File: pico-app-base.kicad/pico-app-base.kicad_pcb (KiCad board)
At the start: 2 copper layers, 53.1 x 61.5 mm, 38 parts, among them J1 Conn_EYESPI, J5 Stemma-QT_Qwicc, J7 JST-PH2 Bat, J9 Alt Bat, Q1 AO3401A, Q2 AO3401A, SW1 SW_ON, SW2 SW_ON, SW3 SW_RST, U1 PCF8563T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

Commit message: added zones and connections
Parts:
- moved SW3 39.0 mm to (125.6, 110.7), turned to 0 degrees
- moved SW1 38.5 mm to (125.6, 102.8), turned to 0 degrees
- moved J1 27.7 mm to (150.2, 134.1), turned to 180 degrees
- moved J5 8.12 mm to (171.3, 79.2), turned to 180 degrees
- moved H2 7.00 mm to (172.4, 86.1)
- moved R3 4.35 mm to (164.8, 87.5)
- moved R4 4.30 mm to (164.8, 85.0)
- moved J7 2.30 mm to (128.3, 96.3)
- moved J9 2.30 mm to (128.7, 97.8)
- moved JP3 1.33 mm to (127.8, 87.8)
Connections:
- C1 pad 1: +BAT -> +BATT
- C2 pad 1: +BAT -> +BATT
- J7 pad 1: +BATT -> Net-(J7-Pin_1)
- J9 pad 1: +BATT -> Net-(J7-Pin_1)
- JP3 pad 1: +BAT -> Net-(J7-Pin_1)
- Q2 pad 2: +BAT -> +BATT
- R2 pad 1: +BAT -> +BATT
- SW2 pad 3: +BAT -> Net-(J7-Pin_1)
- U1 pad 8: +BAT -> +BATT
- U2 pad 7: +BAT -> +BATT
- U2 pad 8: +BAT -> +BATT
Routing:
- net GND: track 0.00 -> 101.2 mm, vias 0 -> 21
- net +3V3: track 112.2 -> 180.7 mm, vias 0 -> 4
- net ~{INT}: track 8.06 -> 42.1 mm
- net +BATT: track 30.5 -> 50.0 mm, vias 0 -> 7
- net Net-(J7-Pin_1): track 0.00 -> 17.3 mm
- net RUN: track 0.00 -> 16.2 mm
- net +BAT: track 8.40 -> 0.00 mm
- net VBUS: track 17.3 -> 12.4 mm, vias 0 -> 6
- net SCL: track 14.8 -> 18.7 mm, vias 3 -> 1
- net SDA: track 14.9 -> 17.8 mm, vias 0 -> 2
- net -BATT: track 16.2 -> 13.9 mm
- net Display_CS: track 0.00 -> 1.69 mm
- net MISO0: track 34.5 -> 36.1 mm
- added copper zone on B.Cu, net +BATT
- added copper zone on F.Cu, net +BATT
- added copper zone on F.Cu, net GND
- added copper zone on B.Cu, net VBUS
- added copper zone on F.Cu, net VBUS

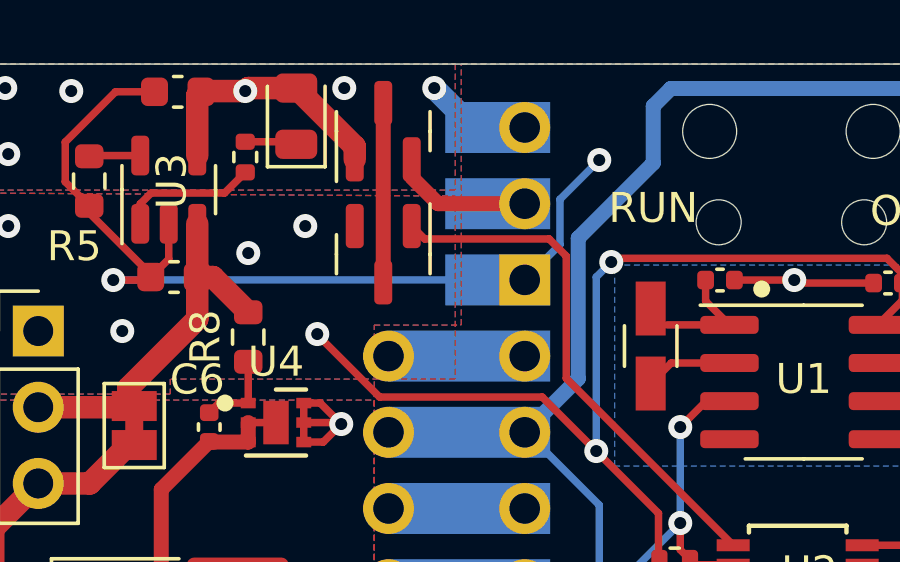
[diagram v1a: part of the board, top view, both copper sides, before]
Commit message: switched order of mosfets
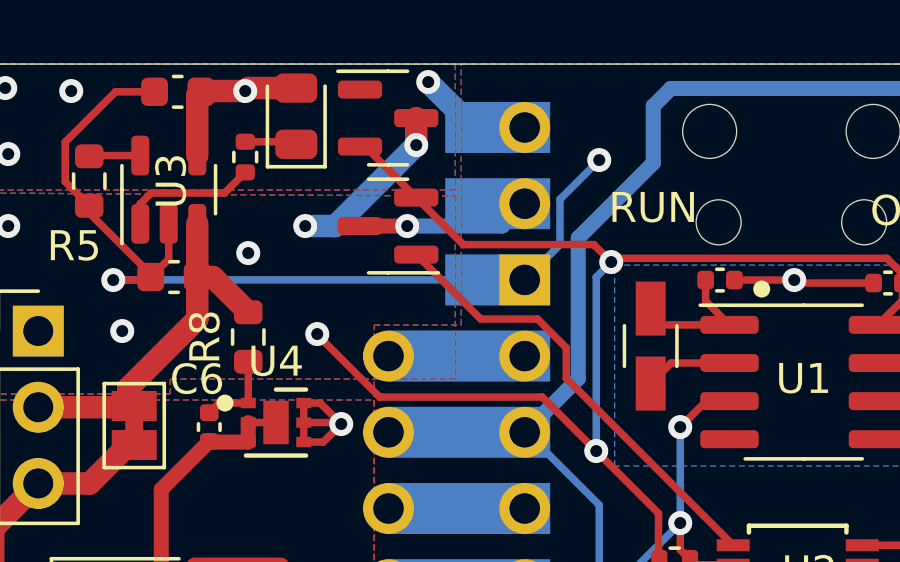
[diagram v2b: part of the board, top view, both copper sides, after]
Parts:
- moved Q2 0.95 mm to (136.3, 81.2), turned to 180 degrees
- moved Q1 0.47 mm to (136.3, 77.6), turned to 0 degrees
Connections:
- C1 pad 1: +BATT -> VCC
- C2 pad 1: +BATT -> VCC
- Q1 pad 2: VSYS -> VCC
- Q1 pad 3: Net-(Q1-D) -> +BATT
- Q2 pad 2: +BATT -> VCC
- Q2 pad 3: Net-(Q1-D) -> VSYS
- R2 pad 1: +BATT -> VCC
- U1 pad 8: +BATT -> VCC
- U2 pad 7: +BATT -> VCC
- U2 pad 8: +BATT -> VCC
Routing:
- net VCC: track 0.00 -> 47.5 mm, vias 0 -> 3
- net +BATT: track 50.0 -> 17.9 mm, vias 7 -> 5
- net Net-(Q1-D): track 5.98 -> 0.00 mm
- net VBUS: track 12.4 -> 9.19 mm, vias 6 -> 5
- net ~{PC_GATE}: track 17.5 -> 15.2 mm
- net VSYS: track 4.13 -> 5.91 mm, vias 0 -> 1

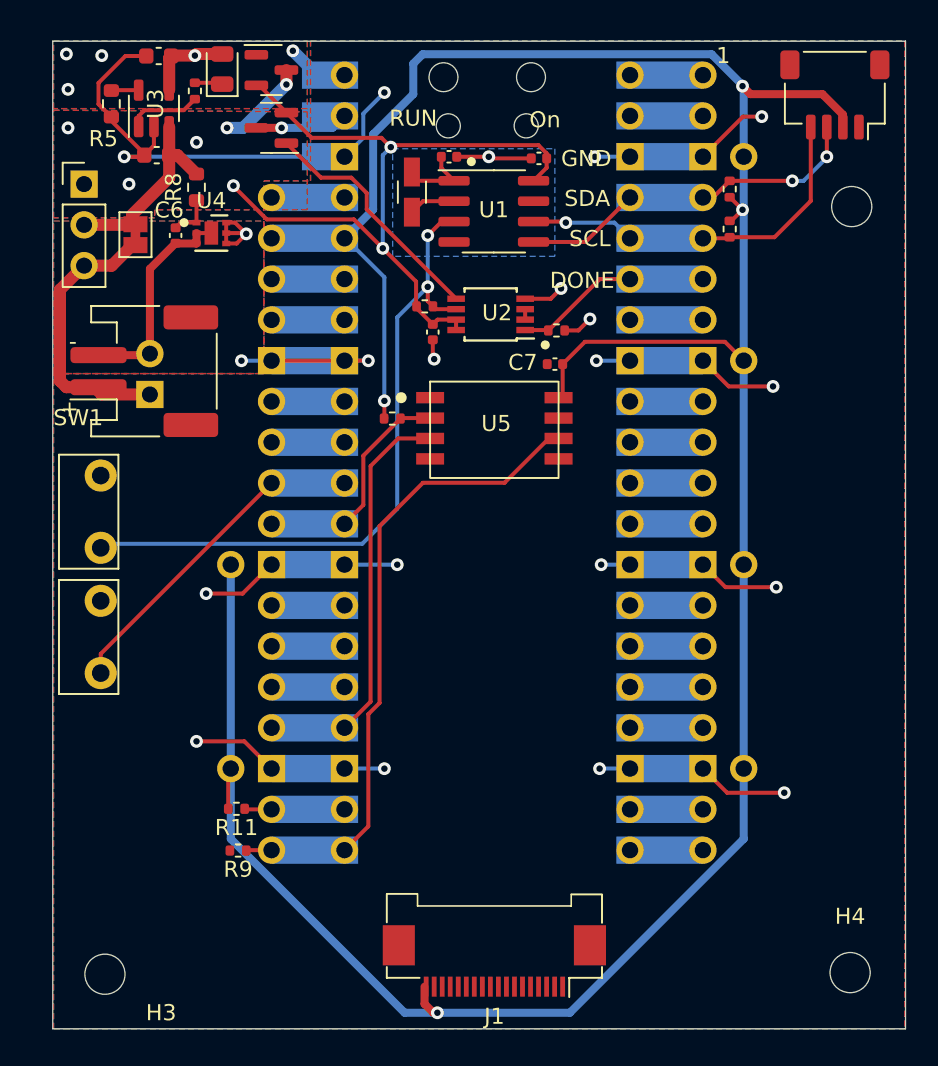
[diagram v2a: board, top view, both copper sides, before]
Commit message: added I2C-grove, completed routing
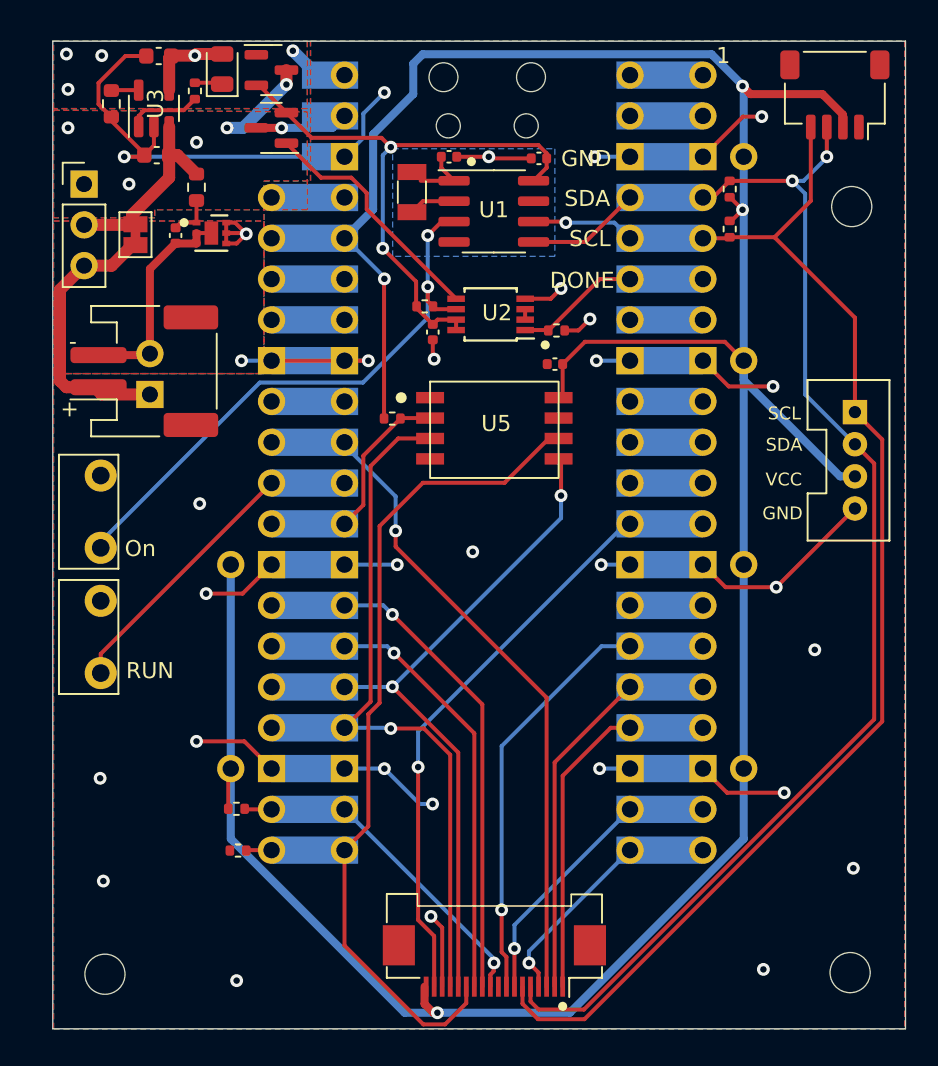
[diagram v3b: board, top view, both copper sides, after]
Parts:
- added J3: Grove, user:grove_vertical, F.Cu at (172.6, 101.9)
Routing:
- net SDA: track 17.8 -> 83.5 mm
- net SCL: track 18.7 -> 83.2 mm
- net MOSI0: track 0.00 -> 42.0 mm, vias 0 -> 2
- net Display_BUSY: track 0.00 -> 39.1 mm, vias 0 -> 1
- net GP9: track 0.00 -> 34.9 mm, vias 0 -> 1
- net Display_RST: track 0.00 -> 28.7 mm, vias 0 -> 1
- net Display_DC: track 0.00 -> 26.1 mm, vias 0 -> 1
- net GP11: track 0.00 -> 25.7 mm, vias 0 -> 1
- net SCLK0: track 21.4 -> 43.1 mm, vias 0 -> 1
- net GP12: track 0.00 -> 20.6 mm
- net GP13: track 0.00 -> 18.6 mm
- net MISO0: track 36.1 -> 53.2 mm
- net GND: track 101.2 -> 116.7 mm, vias 21 -> 31
- net Display_CS: track 1.69 -> 16.7 mm, vias 0 -> 1
- net GP14: track 0.00 -> 14.0 mm, vias 0 -> 1
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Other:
- board text added: "VCC"

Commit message: added labels
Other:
- board text added: "D_DC: GP20 MISO: GP16 MOSI: GP19 SCK: GP18 BLITE: GP9"
- board text added: "GPI02: GP13 GPIO1: GP12 BUSY: GP26 INT: GP15 SDA: GP2 SCL: GP3"
- board text added: "T_CS: GP14 M_CS: GP11 S_CS: nc D_CS: GP17 RST: GP21"
- board text removed: "VCC"

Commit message: added battery-fuel gauge
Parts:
- added C8: 100nF, Capacitor_SMD:C_0402_1005Metric, F.Cu at (130.7, 90.6)
- added U7: MAX17048G, user:MAX17048G, F.Cu at (133.1, 90.4)
- moved R2 0.77 mm to (145.2, 92.8), turned to 90 degrees
- moved J7 0.18 mm to (128.3, 96.5)
- moved J9 0.17 mm to (128.7, 98.0)
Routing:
- net SCL: track 83.2 -> 107.8 mm, vias 1 -> 2
- net SDA: track 83.5 -> 102.7 mm, vias 2 -> 4
- net +BATT: track 17.9 -> 27.1 mm, vias 5 -> 6
- net -BATT: track 13.9 -> 20.8 mm
- net ~{PC_GATE}: track 15.2 -> 16.9 mm, vias 0 -> 2
- net VCC: track 36.6 -> 37.7 mm
- net ~{INT}: track 36.5 -> 37.5 mm, vias 2 -> 1
- net +3V3: track 191.2 -> 191.3 mm, vias 4 -> 3
